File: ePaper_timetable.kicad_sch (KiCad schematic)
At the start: 44 parts, among them J1 26 pin FPC connector 0.5 mm p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, J2 Charging input - 5V, J3 Jumpers, J4 Jumpers, J5 Battery connector, Q1 NMOS, Q2 FS8205A, Q3 PMOS, SW1 SW_Push, SW2 SW_Push, SW3 SW_Push, U1 TP4056, U2 DW01A

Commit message: reference board
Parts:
- removed A1: SC0918, Raspberry Pi:MODULE_SC0918, symbol Raspberry_Pi_Pico_W_SC0918:SC0918
- removed Q3: PMOS, symbol Simulation_SPICE:PMOS
- added Q4: PMOS, symbol Simulation_SPICE:PMOS
- added U3: Pico, RPi_Pico:RPi_Pico_SMD_TH, symbol MCU_RaspberryPi_and_Boards:Pico
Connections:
- net 3.3V: now also U3.36 (3V3)
- net EPD_BUSY': now also U3.7 (GPIO5)
- net EPD_CS': now also U3.12 (GPIO9)
- net EPD_DC': now also U3.9 (GPIO6)
- net EPD_DIN': now also U3.15 (GPIO11)
- net EPD_PWR: now also U3.2 (GPIO1)
- net EPD_RST': now also U3.1 (GPIO0)
- net EPD_SCK': now also U3.14 (GPIO10)
- net GND: now also U3.13 (GND), U3.18 (GND), U3.28 (GND), U3.3 (GND), U3.33 (AGND), U3.38 (GND), U3.42 (GND), U3.8 (GND)
- net SW1: now also U3.24 (GPIO18)
- net SW2: now also U3.25 (GPIO19)
- net SW3: now also U3.26 (GPIO20)
- net V_{battery}: now also Q4.1 (D)
- new net: Q4.2 (G), U3.40 (VBUS)
- new net: Q4.3 (S), U3.39 (VSYS)
- no-connect marks 8 -> 30
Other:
- moved on the sheet: C1, C10, C11, C12, C13, C2, C3, C4, C5, C6, C7, C8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

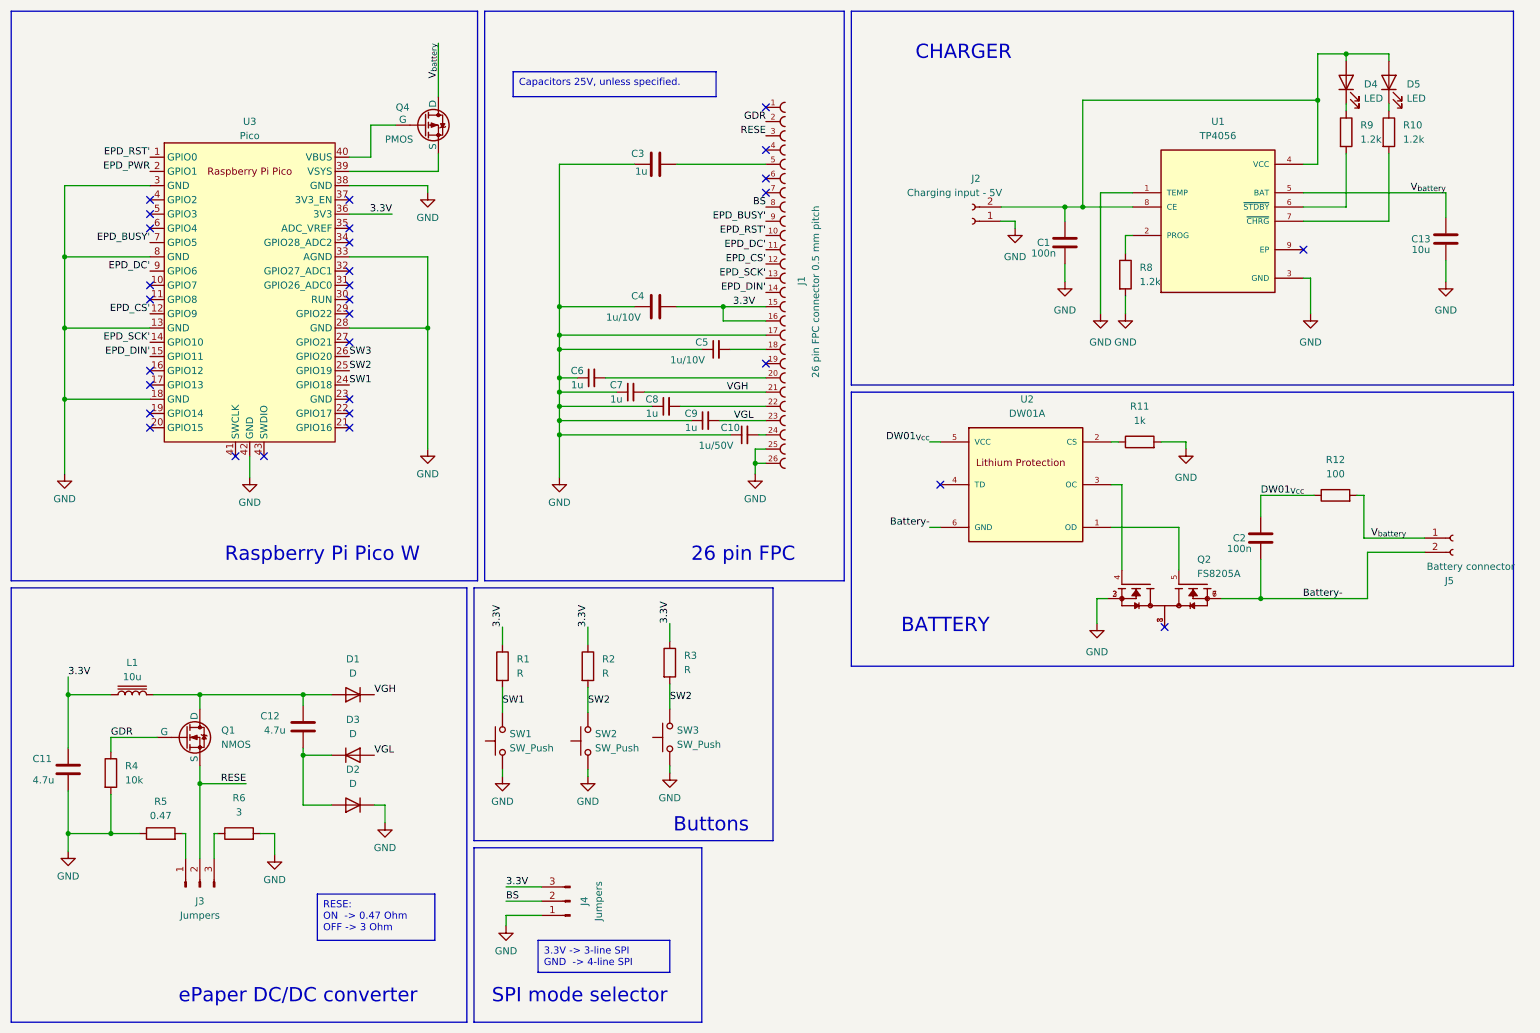
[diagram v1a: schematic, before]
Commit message: schematic update: added footprints
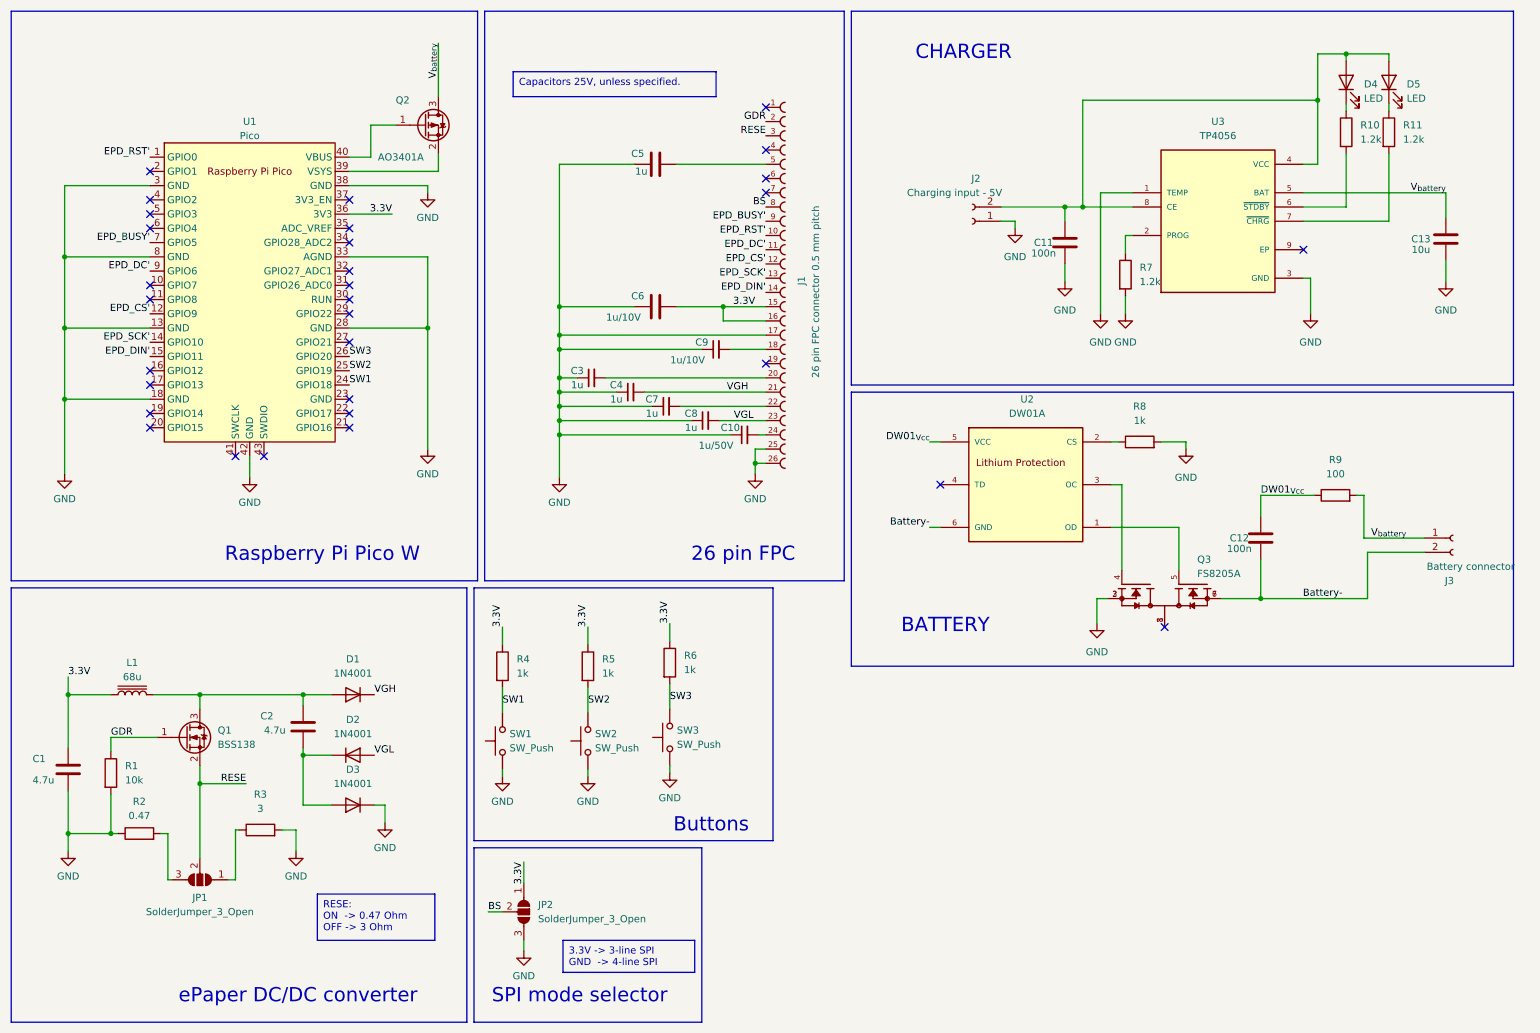
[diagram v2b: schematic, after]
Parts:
- removed D1, D2, D3: D, symbol Device:D
- removed J3, J4: Jumpers, symbol Connector:Conn_01x03_Pin
- removed Q1: NMOS, symbol Simulation_SPICE:NMOS
- removed Q4: PMOS, symbol Simulation_SPICE:PMOS
- added D1, D2, D3: 1N4001, Diode_THT:D_DO-41_SOD81_P10.16mm_Horizontal, symbol Diode:1N4001
- added JP1, JP2: SolderJumper_3_Open, Jumper:SolderJumper-3_P1.3mm_Open_RoundedPad1.0x1.5mm_NumberLabels, symbol Jumper:SolderJumper_3_Open
- added Q1: BSS138, Package_TO_SOT_SMD:SOT-23, symbol Transistor_FET:BSS138
- added Q2: AO3401A, Package_TO_SOT_SMD:SOT-23, symbol Transistor_FET:AO3401A
- C1: renamed from C11; footprint (none) -> Capacitor_SMD:C_1206_3216Metric_Pad1.33x1.80mm_HandSolder
- C10, C13: footprint (none) -> Capacitor_SMD:C_1206_3216Metric_Pad1.33x1.80mm_HandSolder
- C11: renamed from C1; footprint (none) -> Capacitor_SMD:C_0805_2012Metric_Pad1.18x1.45mm_HandSolder
- C12: renamed from C2; footprint (none) -> Capacitor_SMD:C_0805_2012Metric_Pad1.18x1.45mm_HandSolder
- C2: renamed from C12; footprint (none) -> Capacitor_SMD:C_1206_3216Metric_Pad1.33x1.80mm_HandSolder
- C3: renamed from C6; footprint (none) -> Capacitor_SMD:C_1206_3216Metric_Pad1.33x1.80mm_HandSolder
- C4: renamed from C7; footprint (none) -> Capacitor_SMD:C_1206_3216Metric_Pad1.33x1.80mm_HandSolder
- C5: renamed from C3; footprint (none) -> Capacitor_SMD:C_1206_3216Metric_Pad1.33x1.80mm_HandSolder
- C6: renamed from C4; footprint (none) -> Capacitor_SMD:C_1206_3216Metric_Pad1.33x1.80mm_HandSolder
- C7: renamed from C8; footprint (none) -> Capacitor_SMD:C_1206_3216Metric_Pad1.33x1.80mm_HandSolder
- C8: renamed from C9; footprint (none) -> Capacitor_SMD:C_1206_3216Metric_Pad1.33x1.80mm_HandSolder
- C9: renamed from C5; footprint (none) -> Capacitor_SMD:C_1206_3216Metric_Pad1.33x1.80mm_HandSolder
- D4, D5: footprint (none) -> LED_SMD:LED_0805_2012Metric_Pad1.15x1.40mm_HandSolder
- L1: value 10u -> 68u; footprint (none) -> Inductor_SMD:L_Changjiang_FNR6045S
- Q3: renamed from Q2; footprint FS8205A:SOP65P640X120-8N -> Package_SO:TSSOP-8_4.4x3mm_P0.65mm
- R1: renamed from R4; footprint (none) -> Resistor_SMD:R_0805_2012Metric_Pad1.20x1.40mm_HandSolder
- R10: renamed from R9; footprint (none) -> Resistor_SMD:R_0805_2012Metric_Pad1.20x1.40mm_HandSolder
- R11: renamed from R10; footprint (none) -> Resistor_SMD:R_0805_2012Metric_Pad1.20x1.40mm_HandSolder
- R2: renamed from R5; footprint (none) -> Resistor_SMD:R_0805_2012Metric_Pad1.20x1.40mm_HandSolder
- R3: renamed from R6; footprint (none) -> Resistor_SMD:R_0805_2012Metric_Pad1.20x1.40mm_HandSolder
- R4: renamed from R1; value R -> 1k; footprint (none) -> Resistor_SMD:R_0805_2012Metric_Pad1.20x1.40mm_HandSolder
- R5: renamed from R2; value R -> 1k; footprint (none) -> Resistor_SMD:R_0805_2012Metric_Pad1.20x1.40mm_HandSolder
- R6: renamed from R3; value R -> 1k; footprint (none) -> Resistor_SMD:R_0805_2012Metric_Pad1.20x1.40mm_HandSolder
- R7: renamed from R8; footprint (none) -> Resistor_SMD:R_0805_2012Metric_Pad1.20x1.40mm_HandSolder
- R8: renamed from R11; footprint (none) -> Resistor_SMD:R_0805_2012Metric_Pad1.20x1.40mm_HandSolder
- R9: renamed from R12; footprint (none) -> Resistor_SMD:R_0805_2012Metric_Pad1.20x1.40mm_HandSolder
- SW1, SW2, SW3: footprint (none) -> Button_Switch_THT:SW_PUSH_6mm_H7.3mm
- U1: renamed from U3; footprint RPi_Pico:RPi_Pico_SMD_TH -> MCU_RaspberryPi_and_Boards:RPi_Pico_SMD_TH
- U2: footprint DW01A:SOT23-6 -> Package_TO_SOT_SMD:SOT-23-6_Handsoldering
- U3: renamed from U1; footprint TP4056:SOP127P600X175-9N -> Package_SO:HTSOP-8-1EP_3.9x4.9mm_P1.27mm_EP2.4x3.2mm_ThermalVias
- renumbered J5 to J3
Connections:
- net 3.3V: now also JP2.1 (A)
- net BS: now also JP2.2 (C)
- net GDR: now also Q1.1 (G)
- net GND: now also D3.1 (K), JP2.3 (B)
- net RESE: now also JP1.2 (C), Q1.2 (S)
- net SW2: no longer R6.2, SW3.2
- net SW3: now also R6.2, SW3.2
- net VGH: now also D1.1 (K)
- net VGL: now also D2.2 (A)
- net V_{battery}: now also Q2.3 (D)
- net at U1.40 (VBUS): now also Q2.1 (G)
- net at U1.39 (VSYS): now also Q2.2 (S)
- net at C2.2, L1.2: now also D1.2 (A), Q1.3 (D)
- net at C2.1: now also D2.1 (K), D3.2 (A)
- net at R2.2: now also JP1.3 (B)
- net at R3.1: now also JP1.1 (A)
- net EPD_PWR: no longer names the net of U1.2 (GPIO1)
- no-connect marks 30 -> 31
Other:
- company: (none) -> KNE AGH
- title: (none) -> ePaper Timetable
- moved on the sheet: R2, R3

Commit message: charging circuit footprints added
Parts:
- D1, D2, D3: footprint Diode_THT:D_DO-41_SOD81_P10.16mm_Horizontal -> Diode_SMD:D_0805_2012Metric_Pad1.15x1.40mm_HandSolder
- J1: footprint 68712614522:68712614522 -> FPC conn:68712614522
- J3: footprint (none) -> Connector_JST:JST_EH_S2B-EH_1x02_P2.50mm_Horizontal
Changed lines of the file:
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@@
       (effects (font (size 1.27 1.27)))
     )
-    (property "Footprint" "Diode_THT:D_DO-41_SOD81_P10.16mm_Horizontal" (at 75.565 155.575 0)
+    (property "Footprint" "Diode_SMD:D_0805_2012Metric_Pad1.15x1.40mm_HandSolder" (at 75.565 155.575 0)
       (effects (font (size 1.27 1.27)) hide)
     )
@@
       (effects (font (size 1.27 1.27)) (justify left))
     )
-    (property "Footprint" "68712614522:68712614522" (at 156.845 61.595 0)
+    (property "Footprint" "FPC conn:68712614522" (at 156.845 61.595 0)
       (effects (font (size 1.27 1.27)) (justify bottom) hide)
     )
@@
       (effects (font (size 1.27 1.27)))
     )
-    (property "Footprint" "" (at 271.78 107.95 0)
+    (property "Footprint" "Connector_JST:JST_EH_S2B-EH_1x02_P2.50mm_Horizontal" (at 271.78 107.95 0)
       (effects (font (size 1.27 1.27)) hide)
     )
@@
       (effects (font (size 1.27 1.27)))
     )
-    (property "Footprint" "Diode_THT:D_DO-41_SOD81_P10.16mm_Horizontal" (at 75.565 146.685 0)
+    (property "Footprint" "Diode_SMD:D_0805_2012Metric_Pad1.15x1.40mm_HandSolder" (at 75.565 146.685 0)
       (effects (font (size 1.27 1.27)) hide)
     )
@@
       (effects (font (size 1.27 1.27)))
     )
-    (property "Footprint" "Diode_THT:D_DO-41_SOD81_P10.16mm_Horizontal" (at 75.565 135.89 0)
-      (effects (font (size 1.27 1.27)) hide)
-    )
+    (property "Footprint" "Diode_SMD:D_0805_2012Metric_Pad1.15x1.40mm_HandSolder" (at 75.565 135.89 0)
+      (effects (font (size 1.27 1.27)) hide)
+    )

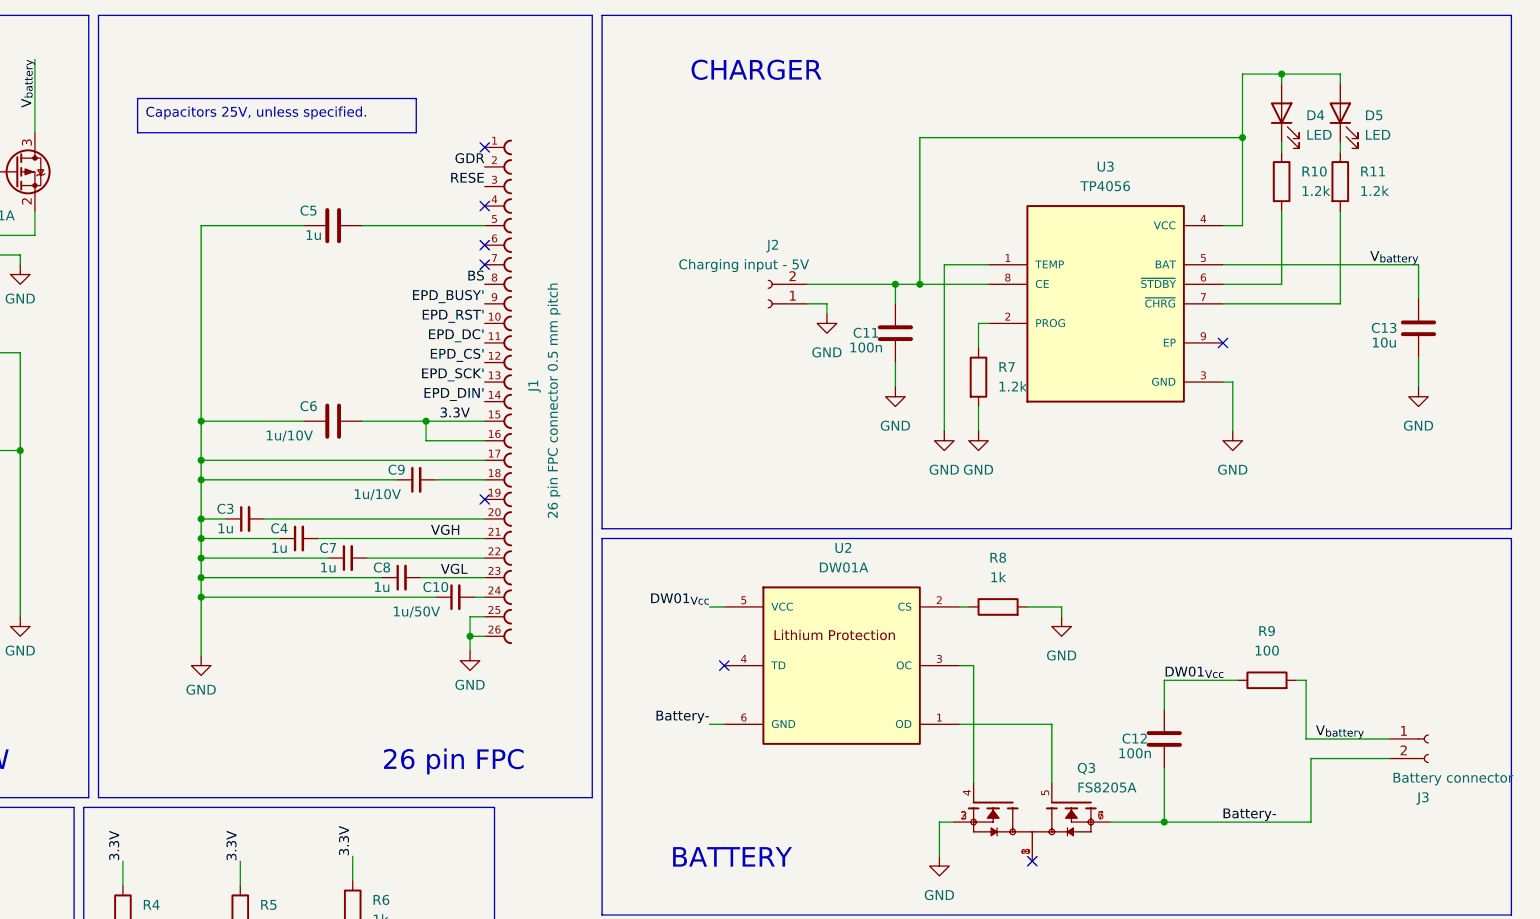
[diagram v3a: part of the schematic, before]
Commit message: Adding FPC footprints libraries.
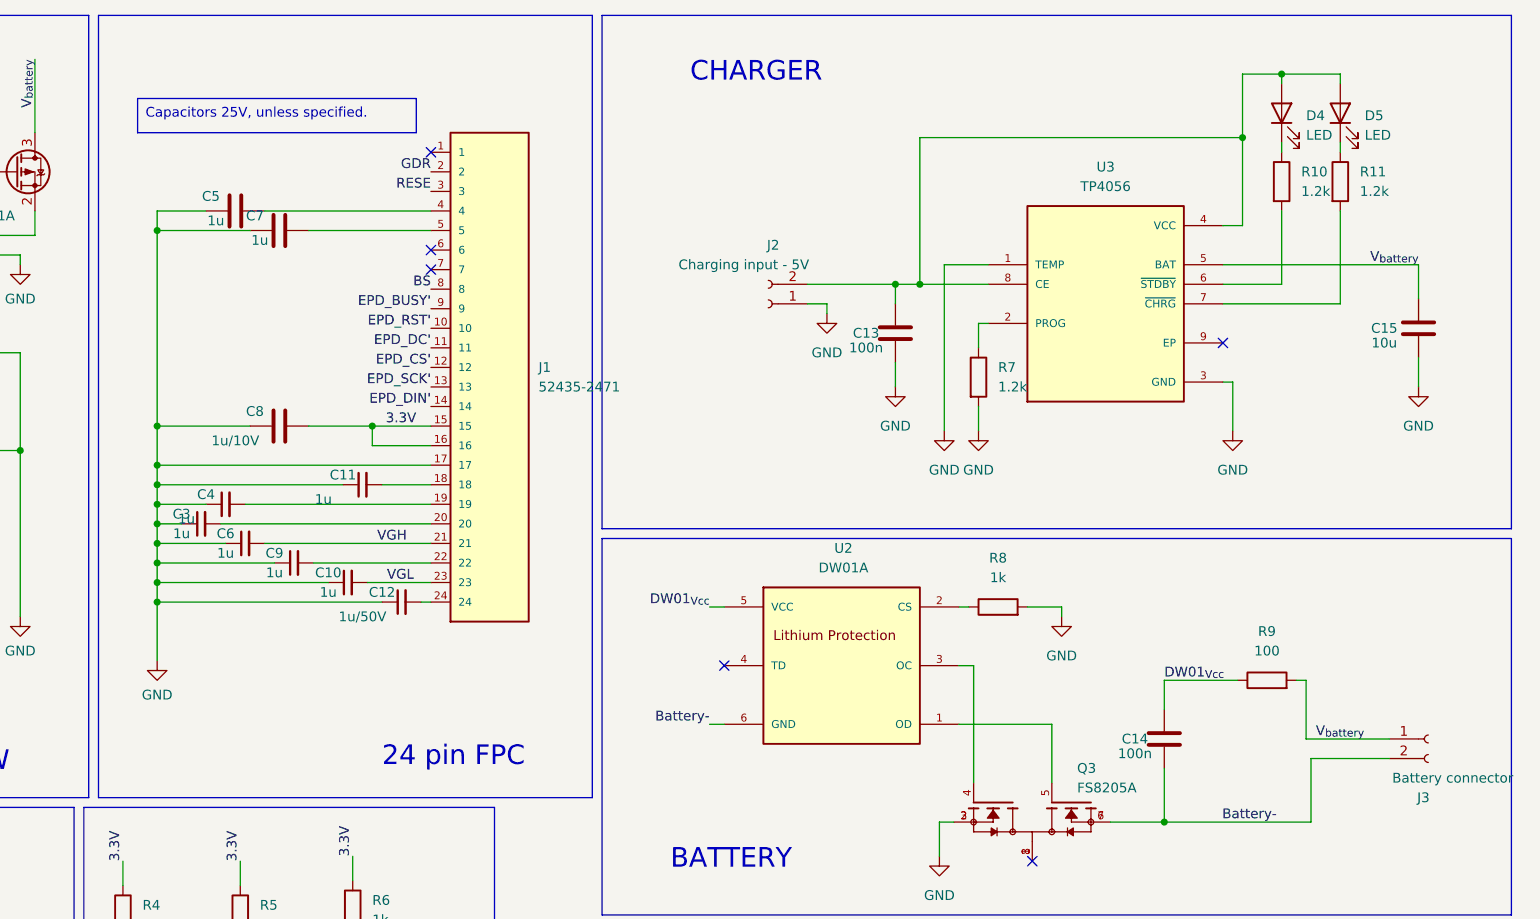
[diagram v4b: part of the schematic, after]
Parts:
- removed J1: 26 pin FPC connector 0.5 mm pitch, FPC conn:68712614522, symbol 68712614522:68712614522
- added C4: 1u, Capacitor_SMD:C_1206_3216Metric_Pad1.33x1.80mm_HandSolder, symbol Device:C_Small
- added C5: 1u, Capacitor_SMD:C_1206_3216Metric_Pad1.33x1.80mm_HandSolder, symbol Device:C
- added J1: 52435-2471, 52435-2471:MOLEX_52435-2471, symbol 52435-2471:52435-2471
- C11: renamed from C9; value 1u/10V -> 1u
- renumbered C8 to C10, C10 to C12, C11 to C13, C12 to C14, C13 to C15, C4 to C6, C5 to C7, C6 to C8, C7 to C9
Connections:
- net 3.3V: now also J1.15, J1.16
- net BS: now also J1.8
- net EPD_BUSY': now also J1.9
- net EPD_CS': now also J1.12
- net EPD_DC': now also J1.11
- net EPD_DIN': now also J1.14
- net EPD_RST': now also J1.10
- net EPD_SCK': now also J1.13
- net GDR: now also J1.2
- net GND: now also C4.1, C5.1, J1.17
- net RESE: now also J1.3
- net VGH: now also J1.21
- net VGL: now also J1.23
- net at C12.2: now also J1.24
- net at C9.2: now also J1.22
- net at C11.2: now also J1.18
- net at C3.2: now also J1.20
- net at C7.2: now also J1.5
- new net: C4.2, J1.19
- new net: C5.2, J1.4
- no-connect marks 31 -> 29
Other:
- note added: "24 pin FPC"
- note removed: "26 pin FPC"
- moved on the sheet: C10, C11, C12, C3, C6, C7, C8, C9
